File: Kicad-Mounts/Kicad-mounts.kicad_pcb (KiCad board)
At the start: 2 copper layers, 25 x 41.2 mm, 8 parts, among them P1 CONN_10, P2 CONN_10, P3 CONN_6X2, P4 CONN_3, P5 CONN_3, P6 CONN_3

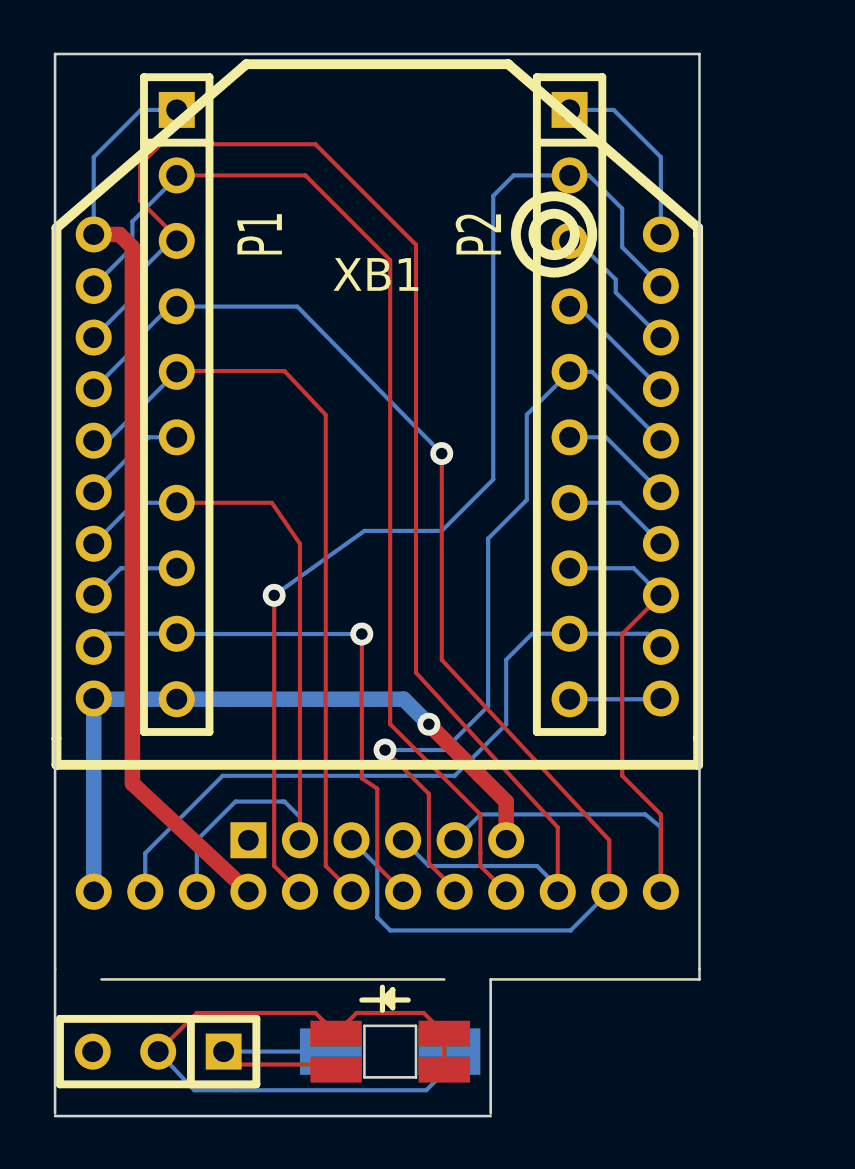
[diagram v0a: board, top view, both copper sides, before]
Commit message: Correct some wiring and ground connection errors in the main board PCB. Reduce size of the LED mount to fit inside meter.
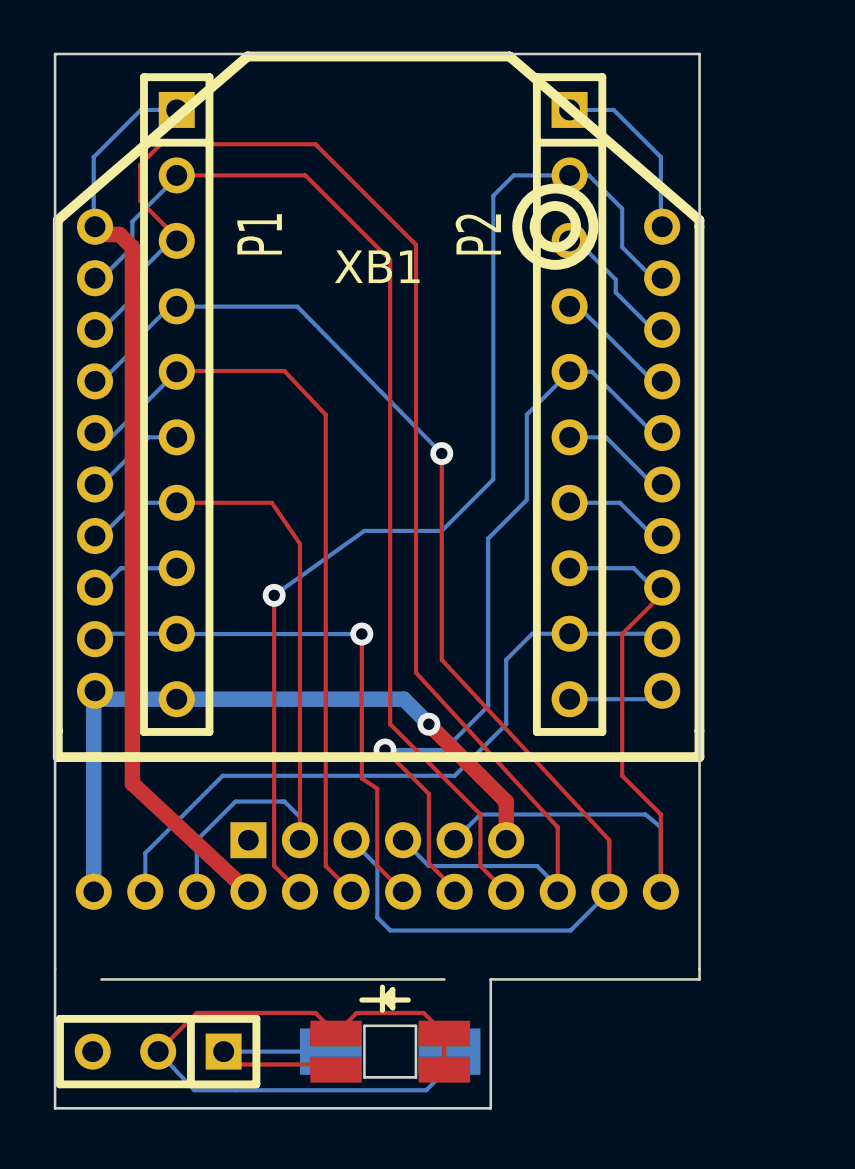
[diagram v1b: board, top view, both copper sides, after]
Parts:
- XB1: footprint Imciner:XBee -> Photodiode:XBee
- moved XB1 0.30 mm to (180.6, 94.7)
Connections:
- D1 pad 3: Net-(D1-Pad1) -> (no net)
- D1 pad 4: Net-(D1-Pad2) -> (no net)
- D1 pad 5: Net-(D1-Pad1) -> (no net)
- D1 pad 6: Net-(D1-Pad1) -> (no net)
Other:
- board size 25 x 41.2 mm -> 25 x 40.9 mm

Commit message: Swap over Tx and Rx
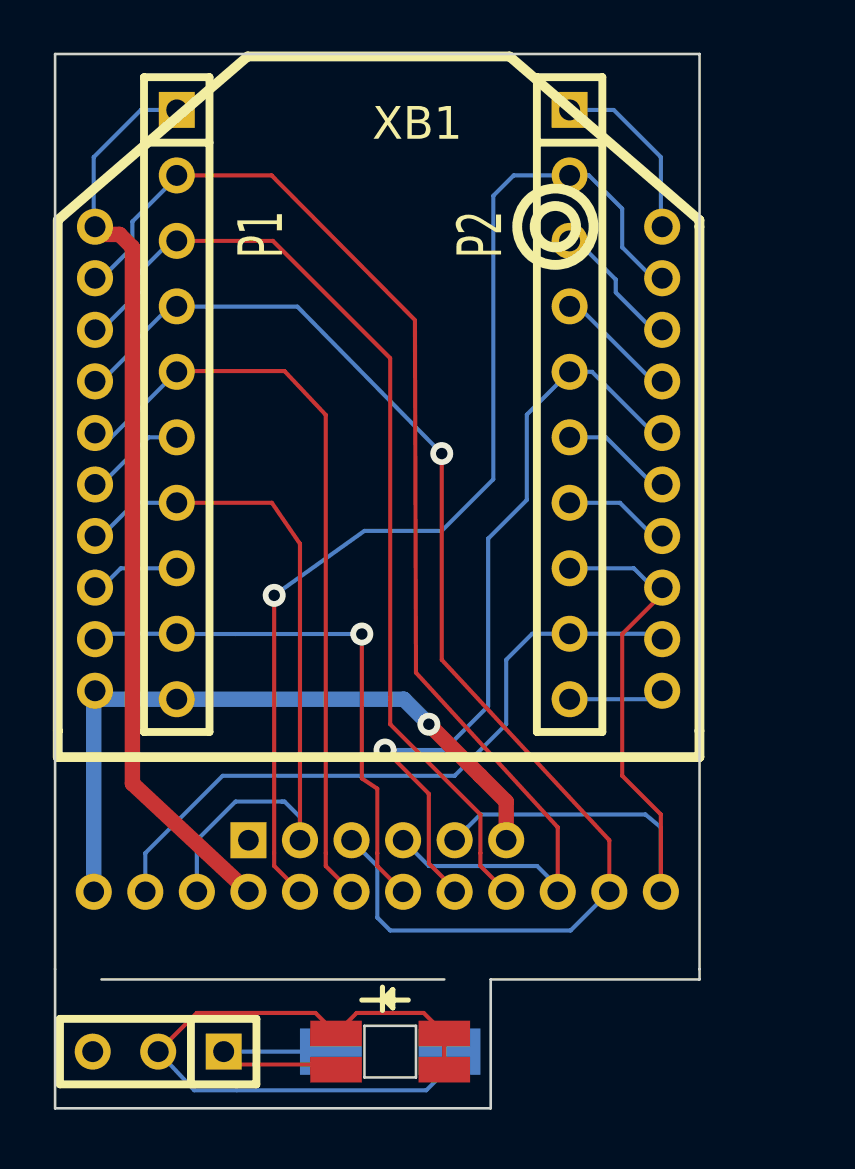
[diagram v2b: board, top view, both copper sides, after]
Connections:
- P1 pad 2: /Tx -> /Rx
- P1 pad 3: /Rx -> /Tx
- XB1 pad 2: /Tx -> /Rx
- XB1 pad 3: /Rx -> /Tx
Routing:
- net /Rx: track 55.7 -> 48.5 mm
- net /Tx: track 41.6 -> 38.1 mm

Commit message: Start of new mounts board with corrected XBee footprint. XBee reversed and lowered to make the mount board shorter.
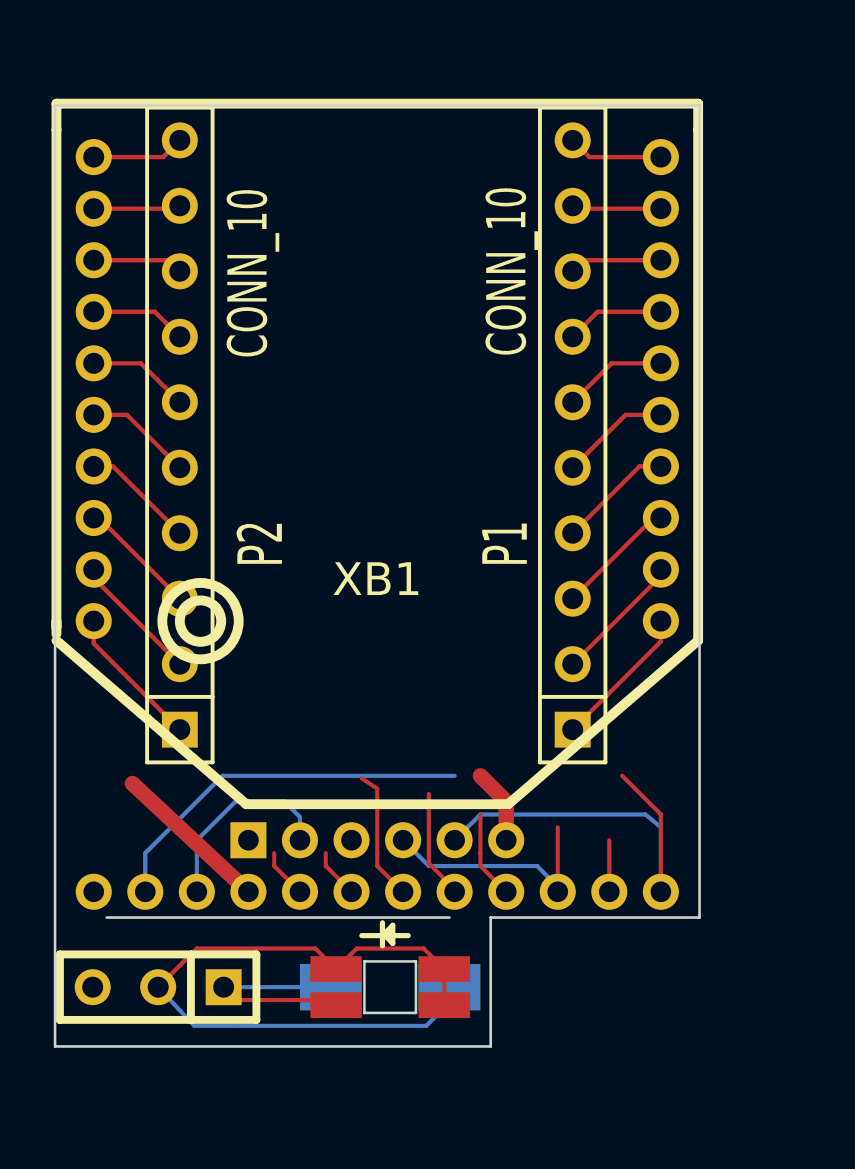
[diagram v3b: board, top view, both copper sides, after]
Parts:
- moved P1 15.4 mm to (188.1, 102.8), turned to 90 degrees
- moved XB1 15.3 mm to (180.5, 110.0), turned to 180 degrees
- moved P2 15.2 mm to (172.8, 102.8), turned to 90 degrees
- moved D1 2.50 mm to (181.1, 124.2)
- moved P6 2.50 mm to (172.0, 124.2)
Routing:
- net /Reset: track 49.3 -> 5.99 mm, vias 1 -> 0
- net /VBatt: track 42.5 -> 6.97 mm, vias 1 -> 0
- net /Rx: track 48.5 -> 14.6 mm
- net /Tx: track 38.1 -> 8.13 mm
- net VCC: track 35.6 -> 11.8 mm
- net /XBee-Reset: track 29.1 -> 6.18 mm
- net /RTS: track 30.3 -> 8.45 mm, vias 1 -> 0
- net GND: track 26.7 -> 6.60 mm, vias 1 -> 0
- net /Bootloader: track 28.8 -> 11.6 mm
- net /Sleep_Rq: track 21.4 -> 8.60 mm, vias 1 -> 0
- net /CTS: track 26.7 -> 18.3 mm
- net /On/Sleep: track 27.3 -> 19.2 mm
- net Net-(P2-Pad1): track 7.30 -> 5.59 mm
- net Net-(P2-Pad3): track 5.39 -> 4.64 mm
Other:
- board size 25 x 40.9 mm -> 25 x 36.5 mm
- net class Default: clearance 0.16 -> 0.17; trace_width 0.16 -> 0.17
- rule trace_clearance: 0.16 -> 0.17
- rule trace_min: 0.16 -> 0.17

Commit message: Rebuilt XBee mount board and generated gerbers for both boards. Remove pngs for now.
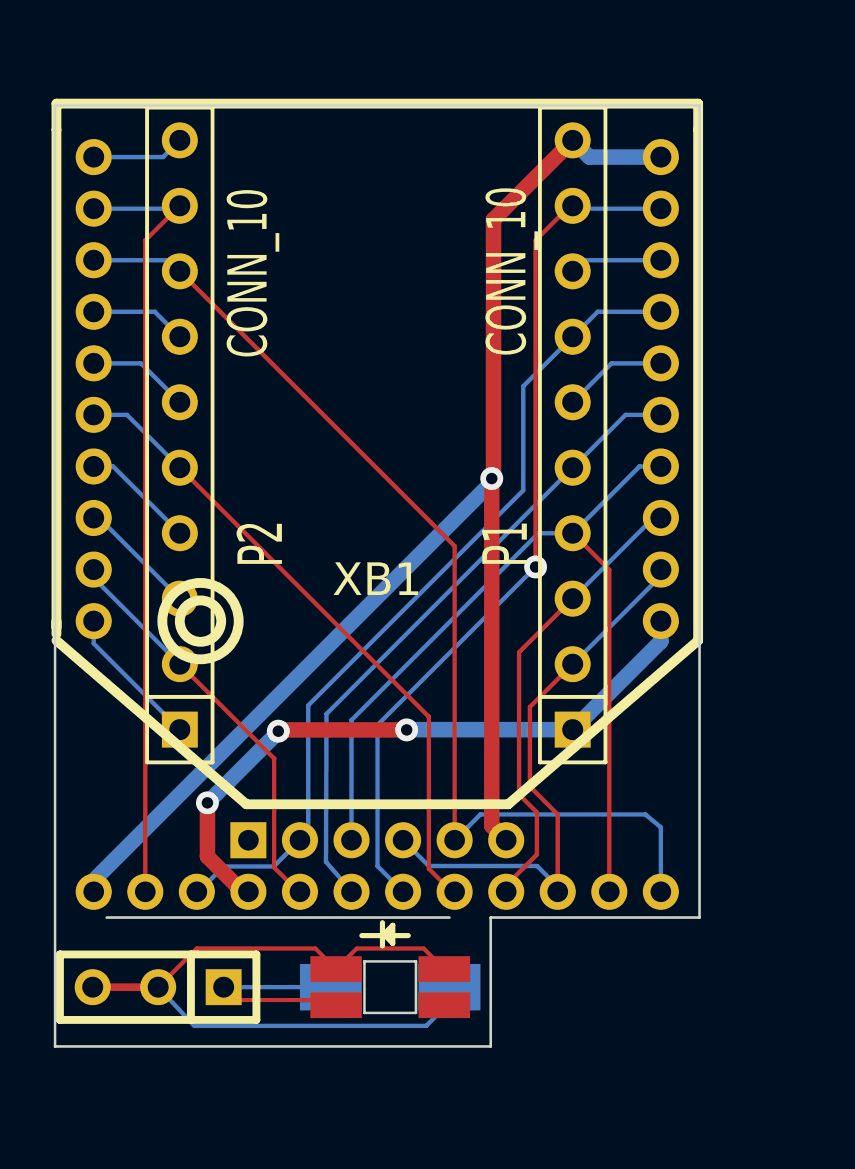
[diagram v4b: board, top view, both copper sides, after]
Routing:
- net GND: track 6.60 -> 54.8 mm, vias 0 -> 1
- net /Reset: track 5.99 -> 35.2 mm
- net /Sleep_Rq: track 8.60 -> 33.8 mm, vias 0 -> 1
- net /On/Sleep: track 19.2 -> 41.7 mm
- net /Bootloader: track 11.6 -> 32.6 mm
- net /XBee-Reset: track 6.18 -> 25.1 mm
- net /RTS: track 8.45 -> 25.1 mm
- net VCC: track 11.8 -> 25.2 mm, vias 0 -> 3
- net /CTS: track 18.3 -> 30.8 mm
- net /Tx: track 8.13 -> 17.7 mm
- net /VBatt: track 6.97 -> 15.8 mm
- net /Rx: track 14.6 -> 22.1 mm
- net Net-(D1-Pad1): track 27.1 -> 28.3 mm
- net Net-(P1-Pad8): track 3.60 -> 4.21 mm

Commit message: Change PCBs to move XBee regulator and caps to the mount board. Change Vcc on mount board to take full battery voltage.
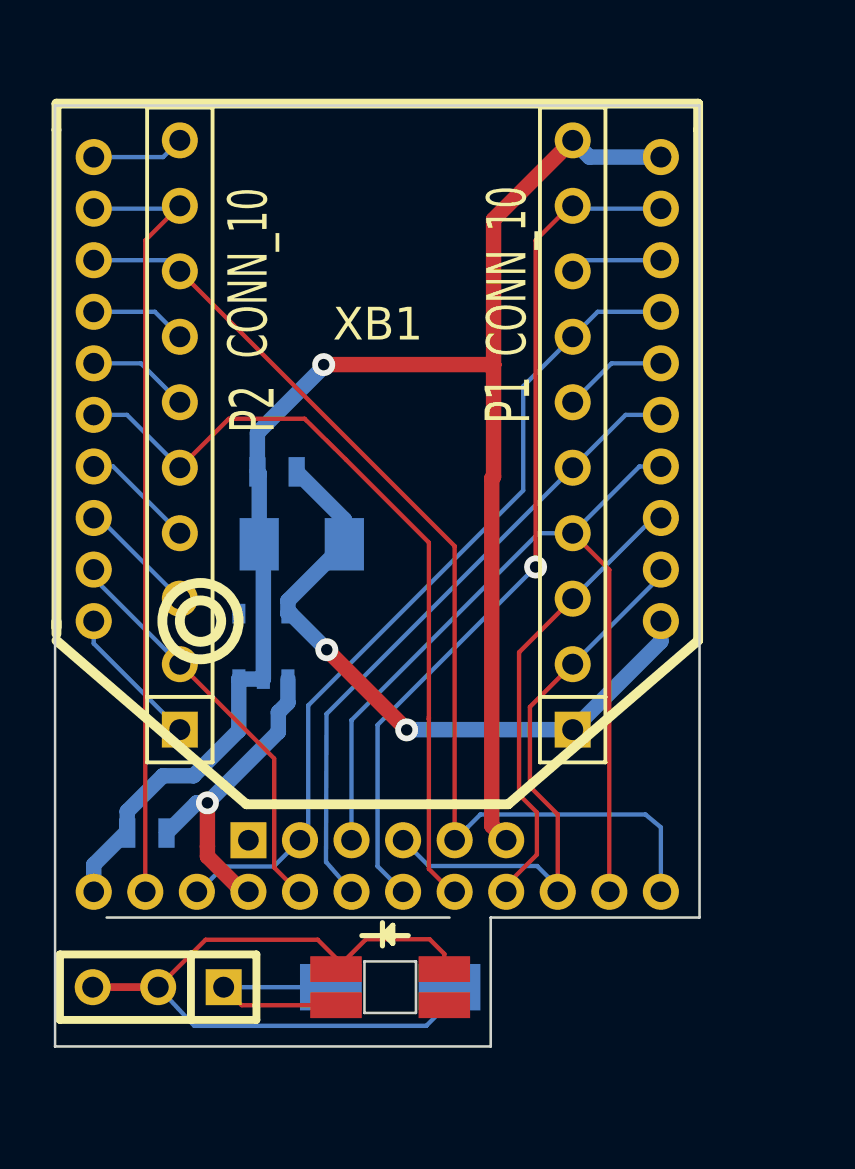
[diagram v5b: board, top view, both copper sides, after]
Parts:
- added C1: 0.47uF, SMD_Packages:SMD-0603_c, B.Cu at (171.6, 118.2)
- added C2: 0.1uF, SMD_Packages:SMD-0603_c, B.Cu at (176.6, 104.2)
- added C3: 10uF, SMD_Packages:SMD-1206_Pol, B.Cu at (177.6, 107.0)
- added U2: TPS77033, SMD_Packages:SOT-23-5, B.Cu at (176.1, 111.0)
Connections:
- P1 pad 1: VCC -> /V3
- XB1 pad 1: VCC -> /V3
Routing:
- net /V3: track 0.00 -> 25.7 mm, vias 0 -> 2
- net VCC: track 25.2 -> 12.4 mm, vias 3 -> 1
- net GND: track 54.8 -> 65.0 mm
- net /RTS: track 25.1 -> 30.8 mm
- net Net-(D1-Pad1): track 28.3 -> 29.4 mm
- net Net-(D1-Pad2): track 8.58 -> 9.23 mm

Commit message: Change orientation of debug connector on main board to fit in housing. Update mounts to narrow down the LED mount
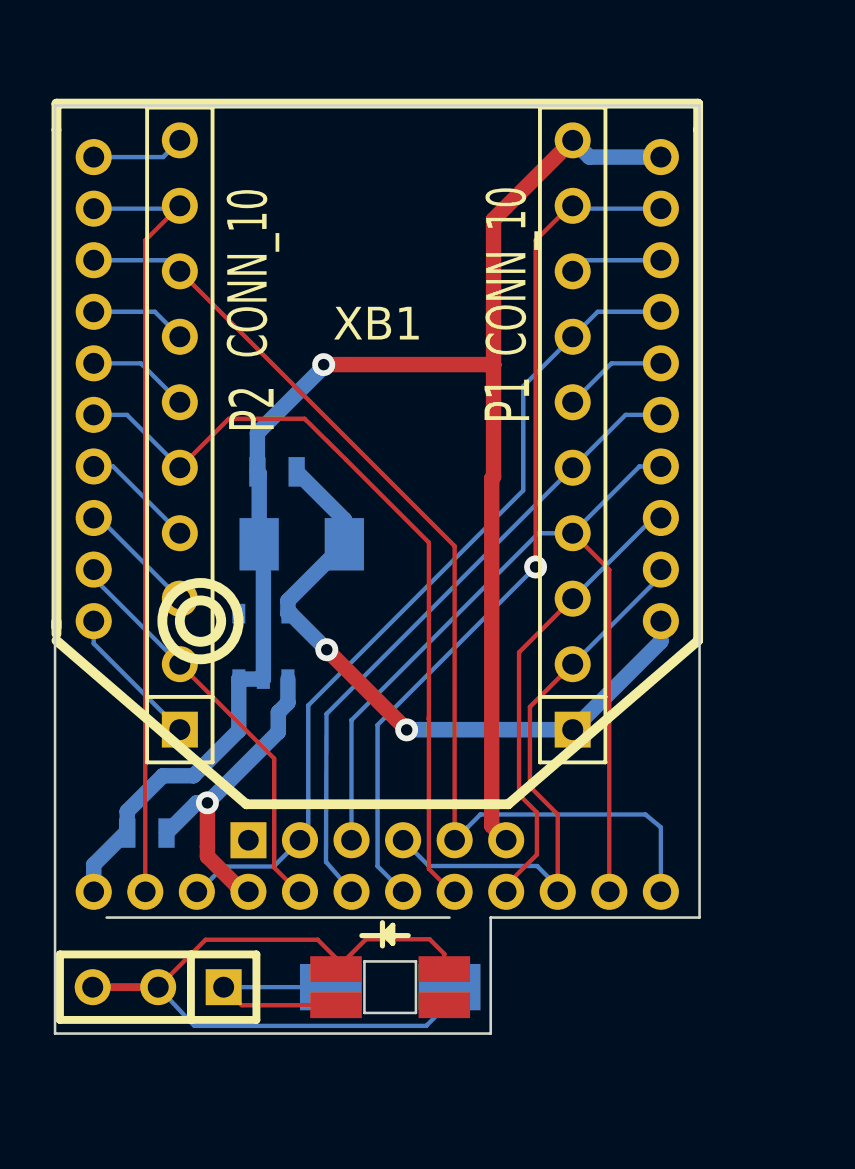
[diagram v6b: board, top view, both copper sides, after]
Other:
- board size 25 x 36.5 mm -> 25 x 36 mm
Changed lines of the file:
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@@
-(kicad_pcb (version 4) (host pcbnew "(2014-08-05 BZR 5054)-product")
+(kicad_pcb (version 4) (host pcbnew 4.0.2-4+6225~38~ubuntu14.04.1-stable)
   (general
     (links 49)
@@
     )
   )
-  (gr_line (start 184.9 121.5) (end 184.9 126.5) (angle 90) (layer Edge.Cuts) (width 0.1))
+  (gr_line (start 184.9 121.5) (end 184.9 126) (angle 90) (layer Edge.Cuts) (width 0.1))
   (gr_line (start 182 123.2) (end 182 125.2) (angle 90) (layer Edge.Cuts) (width 0.1))
   (gr_line (start 180 123.2) (end 180 125.2) (angle 90) (layer Edge.Cuts) (width 0.1))
@@
   (gr_line (start 184.9 121.5) (end 193 121.5) (angle 90) (layer Edge.Cuts) (width 0.1))
   (gr_line (start 193 90) (end 193 121.5) (angle 90) (layer Edge.Cuts) (width 0.1))
-  (gr_line (start 168 126.5) (end 184.9 126.5) (angle 90) (layer Edge.Cuts) (width 0.1))
+  (gr_line (start 168 126) (end 184.9 126) (angle 90) (layer Edge.Cuts) (width 0.1))
   (gr_line (start 168 90) (end 193 90) (angle 90) (layer Edge.Cuts) (width 0.1))
-  (gr_line (start 168 90) (end 168 126.5) (angle 90) (layer Edge.Cuts) (width 0.1))
+  (gr_line (start 168 90) (end 168 126) (angle 90) (layer Edge.Cuts) (width 0.1))
   (segment (start 172 124.2) (end 169.46 124.2) (width 0.3) (layer F.Cu) (net 1))
   (segment (start 173.4 125.7) (end 172 124.2) (width 0.17) (layer B.Cu) (net 1) (status 20))

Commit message: Change mount board to rotate XBee sideways and keep dual row connector only
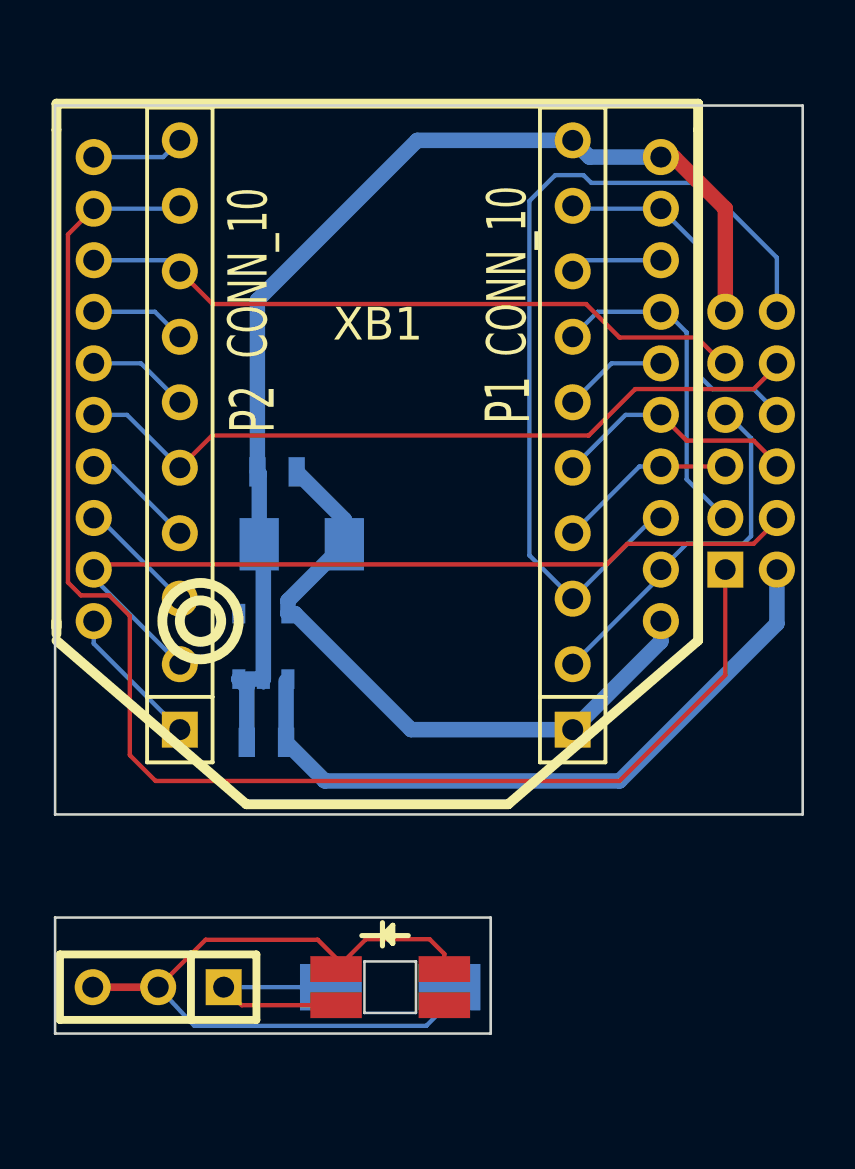
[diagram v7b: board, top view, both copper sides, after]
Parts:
- removed P4, P5: CONN_3, Photodiode:pin_header_2mm_1x3
- moved P3 22.0 mm to (195.0, 103.0), turned to 90 degrees
- moved C1 5.82 mm to (176.2, 114.7)
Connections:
- P3 pad 1: Net-(P3-Pad1) -> /CTS
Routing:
- net /Reset: track 35.2 -> 6.99 mm
- net /CTS: track 30.8 -> 56.2 mm
- net GND: track 65.0 -> 44.5 mm, vias 1 -> 0
- net /Bootloader: track 32.6 -> 13.0 mm
- net /Sleep_Rq: track 33.8 -> 14.5 mm, vias 1 -> 0
- net /VBatt: track 15.8 -> 32.4 mm
- net /Tx: track 17.7 -> 34.3 mm
- net /XBee-Reset: track 25.1 -> 9.66 mm
- net /On/Sleep: track 41.7 -> 26.8 mm
- net VCC: track 12.4 -> 27.1 mm, vias 1 -> 0
- net /Rx: track 22.1 -> 14.3 mm
- net /RTS: track 30.8 -> 29.1 mm
- net /V3: track 25.7 -> 25.8 mm, vias 2 -> 0
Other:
- board size 25 x 36 mm -> 29 x 36 mm
